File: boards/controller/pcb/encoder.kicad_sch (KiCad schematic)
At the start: 10 parts, among them SW401 EC11E15204A3

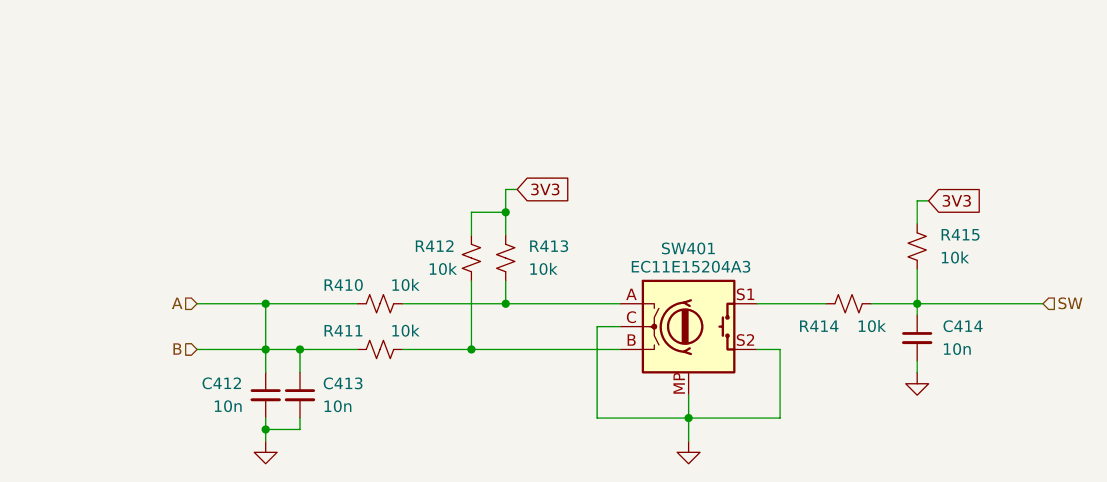
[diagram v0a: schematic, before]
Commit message: controller: pcb: Update schematic
Signed-off-by: Nicholas Loehrke <nicholasnloehrke@gmail.com>
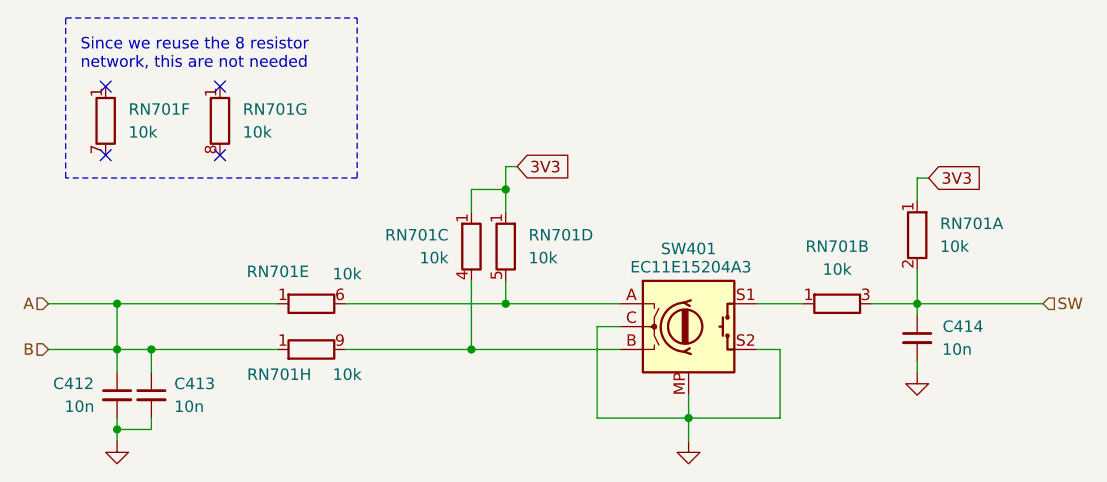
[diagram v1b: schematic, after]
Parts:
- removed R410, R411, R412, R413, R414, R415: 10k, symbol Device:R_Small_US
- added RN701: 10k, Resistor_THT:R_Array_SIP9, symbol Device:R_Network08_Split
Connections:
- net 3V3: now also RN701.1 (R1), RN701.1 (R1), RN701.1 (R1)
- net A: now also RN701.1 (R1), RN701.1 (R1)
- net SW: now also RN701.2 (R1.2), RN701.3 (R2.2)
- net at SW401.B: now also RN701.4 (R3.2), RN701.9 (R8.2)
- net at SW401.A: now also RN701.5 (R4.2), RN701.6 (R5.2)
- net at SW401.S1: now also RN701.1 (R1)
- no-connect marks 0 -> 4
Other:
- note added: "Since we reuse the 8 resistor network, this are not needed"
- moved on the sheet: C412, C413

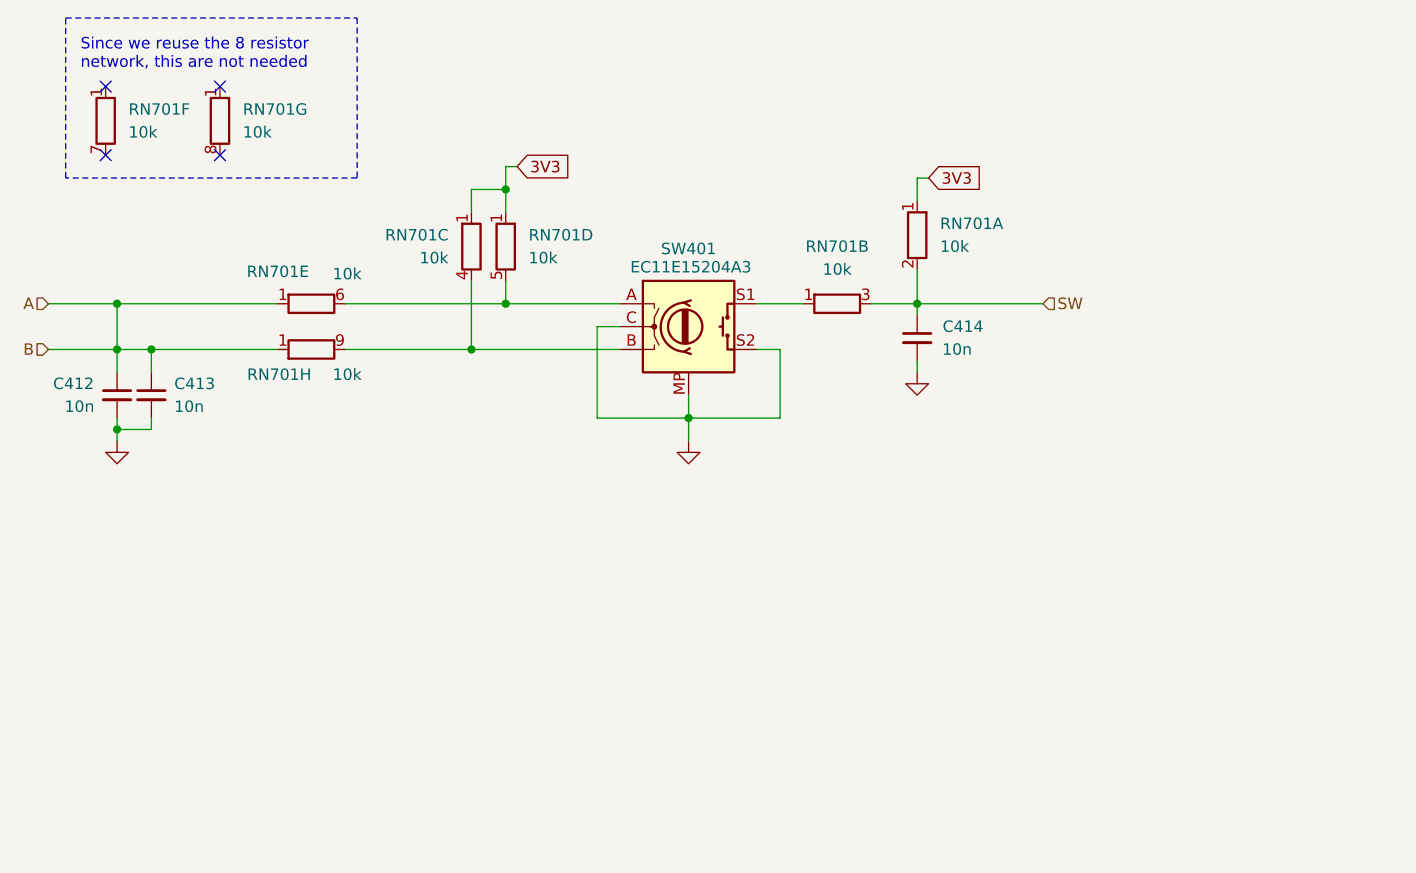
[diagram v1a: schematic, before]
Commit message: controller: pcb: Update schematic
Signed-off-by: Nicholas Loehrke <nicholasnloehrke@gmail.com>
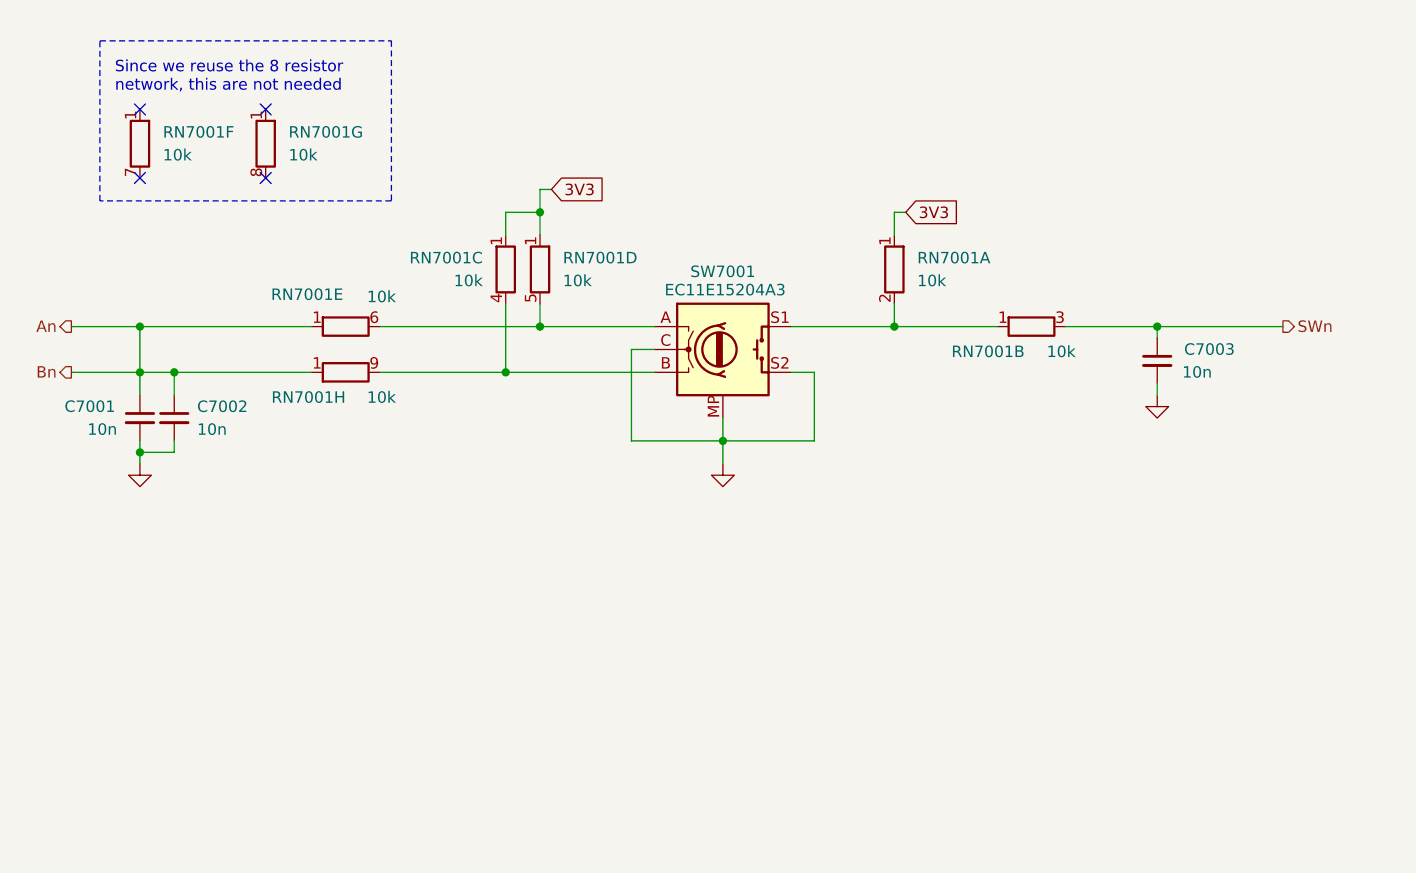
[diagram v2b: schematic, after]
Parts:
- removed unit 1 of RN701
- added unit 1 of RN7001
- renumbered C412 to C7001, C413 to C7002, C414 to C7003, RN701 to RN7001, SW401 to SW7001
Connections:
- net 3V3: now also RN7001.1 (R1)
- net at RN7001.1 (R1), SW7001.S1: now also RN7001.2 (R1.2)
- net A renamed An
- net SW renamed SWn
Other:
- moved on the sheet: C7001, C7002, C7003, RN7001B, RN7001C, RN7001D, RN7001E, RN7001F, RN7001G, RN7001H, SW7001

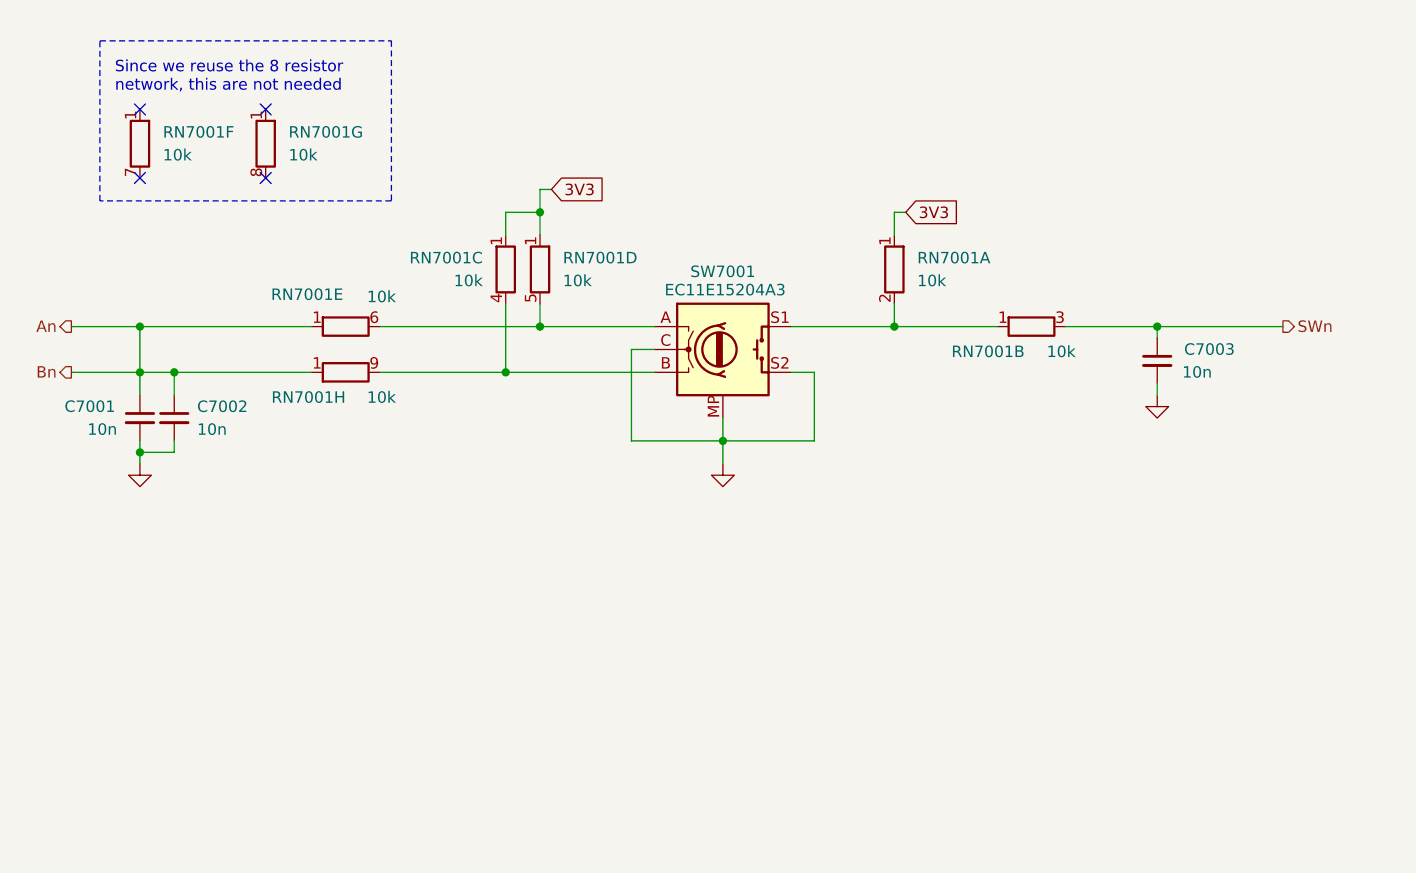
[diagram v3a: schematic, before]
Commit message: controller: pcb: Update schematic
- Add power button pmos gate voltage clamp
- Add TVS diodes on encoders

Signed-off-by: Nicholas Loehrke <nicholasnloehrke@gmail.com>
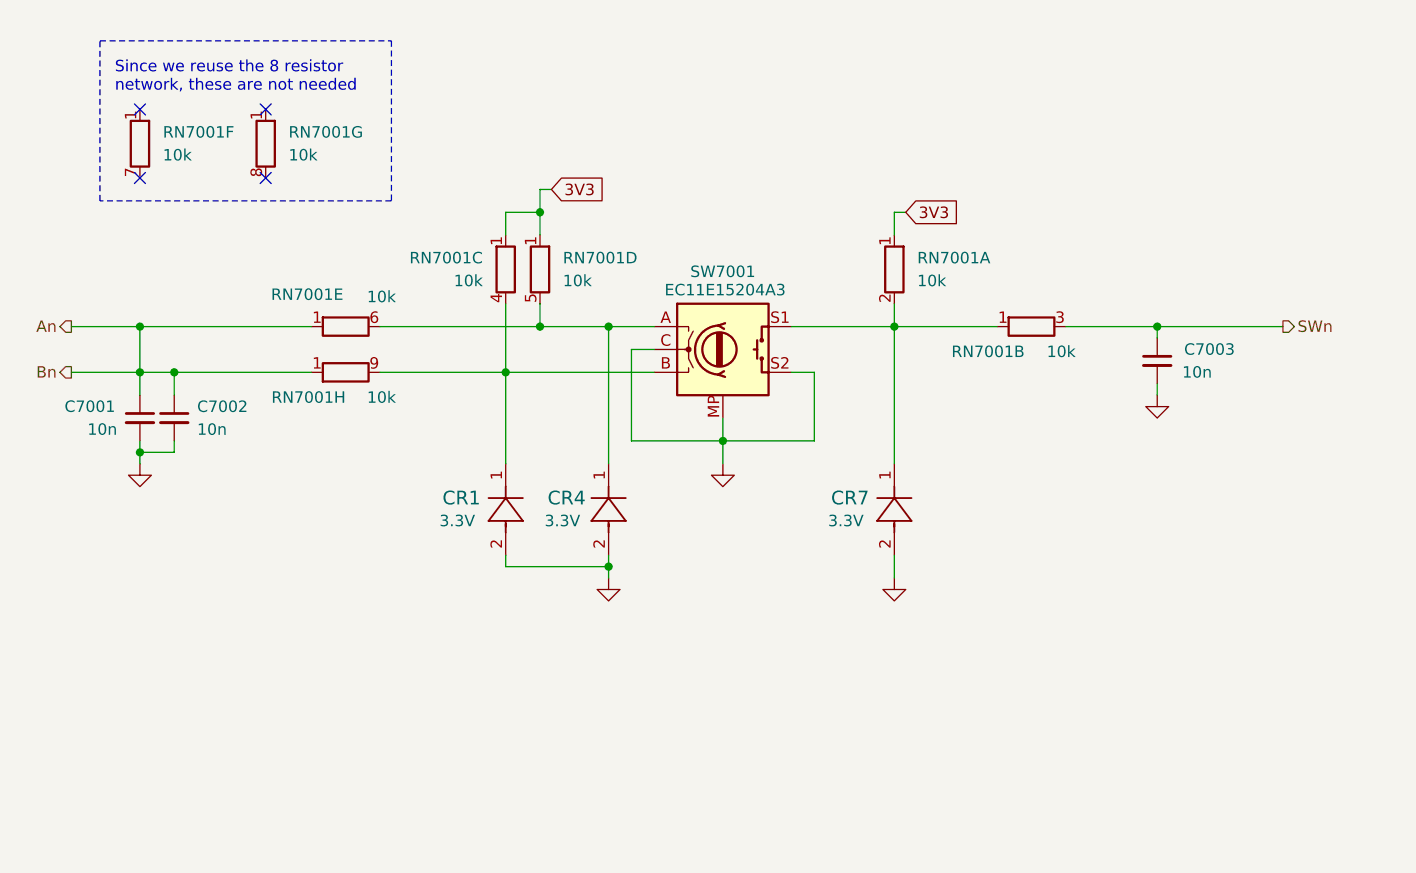
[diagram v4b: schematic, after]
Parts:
- added CR1, CR4, CR7: PJSD03TS-AU_R1_000A1, CR_SOD-523_PNJ, symbol PJSD03TS-AU_R1_000A1:PJSD03TS-AU_R1_000A1
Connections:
- net GND: now also CR1.2, CR4.2, CR7.2
- net at RN7001.5 (R4.2), RN7001.6 (R5.2), SW7001.A: now also CR4.1
- net at RN7001.4 (R3.2), RN7001.9 (R8.2), SW7001.B: now also CR1.1
- net at RN7001.1 (R1), RN7001.2 (R1.2), SW7001.S1: now also CR7.1
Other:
- note added: "Since we reuse the 8 resistor network, these are not needed"
- note removed: "Since we reuse the 8 resistor network, this are not needed"

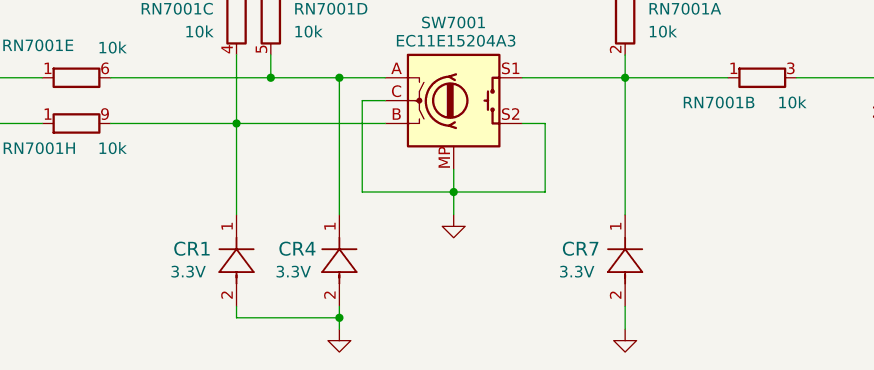
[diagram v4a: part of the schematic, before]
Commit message: controller: pcb: Update schematic
- Add TVS diodes on select MCU pins

Signed-off-by: Nicholas Loehrke <nicholasnloehrke@gmail.com>
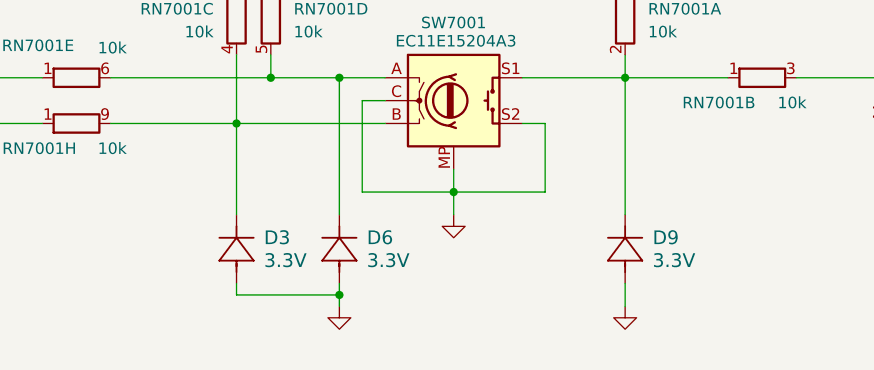
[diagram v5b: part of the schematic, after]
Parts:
- removed CR1, CR4, CR7: PJSD03TS-AU_R1_000A1, CR_SOD-523_PNJ, symbol PJSD03TS-AU_R1_000A1:PJSD03TS-AU_R1_000A1
- added D3, D6, D9: 3.3V, CR_SOD-523_PNJ, symbol PJSD03TS-AU_R1_000A1:PJSD03TS-AU_R1_000A1
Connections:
- net GND: now also D3.2, D6.2, D9.2
- net at RN7001.5 (R4.2), RN7001.6 (R5.2), SW7001.A: now also D6.1
- net at RN7001.4 (R3.2), RN7001.9 (R8.2), SW7001.B: now also D3.1
- net at RN7001.1 (R1), RN7001.2 (R1.2), SW7001.S1: now also D9.1
